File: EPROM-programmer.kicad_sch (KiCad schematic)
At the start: 63 parts, among them J1 ZIF-socket, J2 ISP, J3 DAC_VCC, J4 DAC_B, J5 GND, J6 Barrel_Jack_Switch, J7 VCC_SEL, J8 AMP_VCC, J9 GND, P1 USB-C, Q1 TIP41C, Q2 BC327, Q3 BC337, SW1 SW_Push, U1 ATmega1284-P, U2 MCP2221AxP, U3 MCP4812, U4 LM358, Y1 20M

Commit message: WIP use LM317
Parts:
- removed J7: VCC_SEL, Connector_PinHeader_2.54mm:PinHeader_1x03_P2.54mm_Vertical, symbol Connector:Conn_01x03_Pin
- removed Q1: TIP41C, Package_TO_SOT_THT:TO-220-3_Vertical, symbol Transistor_BJT:TIP41C
- removed Q3: BC337, Package_TO_SOT_THT:TO-92_Inline_Wide, symbol Transistor_BJT:BC337
- removed R18: 2K, Resistor_THT:R_Axial_DIN0207_L6.3mm_D2.5mm_P10.16mm_Horizontal, symbol Device:R
- added C15, C16: 10u, Local:C_Rect_L4.6mm_W3.0mm_P2.50mm_MKS02_FKP02, symbol Device:C_Polarized
- added D8: SB340, Diode_THT:D_DO-201AD_P15.24mm_Horizontal, symbol Diode:B340
- added Q1: BC327, Package_TO_SOT_THT:TO-92_Inline_Wide, symbol Transistor_BJT:BC327
- added U5: ULN2003, Package_DIP:DIP-16_W7.62mm_Socket, symbol Transistor_Array:ULN2003
- added U6: LM317_TO-220, Package_TO_SOT_THT:TO-220-3_Vertical, symbol Regulator_Linear:LM317_TO-220
- J4: value DAC_B -> DAC_VPP
- R15: value 1K -> 5.1K
- R16: value 2K -> 5.1K
- R17: value 2K -> 240
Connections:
- net V_VCC is gone; now on net ZIF_VCC: Q2.1 (C)
- net +28V: now also C15.1, D8.1 (K), U6.3 (VI)
- net AMP_VCC: now also R17.1, C16.1, D8.2 (A), U6.2 (VO)
- net GND: now also C15.2, C16.2, Q1.1 (C), U5.8 (GND)
- net ZIF_VCC_EN: now also U5.1 (I1); no longer R17.1
- net ZIF_VPP_P21_EN: now reaches U1.2 (PB1)
- net ZIF_VPP_P21_EN: now also U5.3 (I3)
- net ZIF_VPP_P22_EN: now reaches U1.3 (PB2)
- net ZIF_VPP_P22_EN: now also U5.5 (I5)
- net ZIF_VPP_P23_EN: now reaches U1.4 (PB3)
- net ZIF_VPP_P23_EN: now also U5.7 (I7)
- net at R15.2: now also U5.16 (O1)
- net at R17.2: now also Q1.3 (E), U6.1 (ADJ)
- net at U4.1: now also Q1.2 (B)
- net DAC_B renamed DAC_VPP
- no-connect marks 10 -> 17
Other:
- moved on the sheet: C12, C6, J1, J5, J8, J9, Q2, R10, R11, R12, R13, R14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

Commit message: Fix some ERC/DRC
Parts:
- added J7: ZIF_VCC, Connector_PinHeader_2.54mm:PinHeader_1x01_P2.54mm_Vertical, symbol Connector:Conn_01x01_Pin
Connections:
- net ZIF_VCC: now also J7.1 (Pin_1)

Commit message: Minor adjustments
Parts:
- R17: value 240 -> 220
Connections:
- net AMP_VCC: no longer R14.2
- net at Q1.3 (E), R17.2, U6.1 (ADJ): now also R14.2
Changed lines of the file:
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@@
 	)
 	(junction
-		(at 154.94 31.75)
-		(diameter 0)
-		(color 0 0 0 0)
-	)
-	(junction
 		(at 190.5 85.09)
 		(diameter 0)
@@
 	)
 	(junction
+		(at 138.43 45.72)
+		(diameter 0)
+		(color 0 0 0 0)
+	)
+	(junction
 		(at 29.21 68.58)
 		(diameter 0)
@@
 	(wire
 		(pts
-			(xy 154.94 31.75) (xy 158.75 31.75)
+			(xy 147.32 31.75) (xy 158.75 31.75)
 		)
 		(stroke
@@
 	(wire
 		(pts
+			(xy 138.43 45.72) (xy 147.32 45.72)
+		)
+		(stroke
+			(width 0)
+			(type default)
+		)
+	)
+	(wire
+		(pts
 			(xy 148.59 187.96) (xy 148.59 189.23)
 		)
@@
 	(wire
 		(pts
+			(xy 138.43 45.72) (xy 129.54 45.72)
+		)
+		(stroke
+			(width 0)
+			(type default)
+		)
+	)
+	(wire
+		(pts
 			(xy 96.52 171.45) (xy 106.68 171.45)
 		)
@@
 	(wire
 		(pts
-			(xy 154.94 31.75) (xy 154.94 63.5)
-		)
-		(stroke
-			(width 0)
-			(type default)
-		)
-	)
-	(wire
-		(pts
 			(xy 271.78 92.71) (xy 271.78 95.25)
 		)
@@
 	(wire
 		(pts
+			(xy 138.43 45.72) (xy 138.43 63.5)
+		)
+		(stroke
+			(width 0)
+			(type default)
+		)
+	)
+	(wire
+		(pts
 			(xy 207.01 148.59) (xy 209.55 148.59)
 		)
@@
 	(wire
 		(pts
-			(xy 147.32 31.75) (xy 154.94 31.75)
-		)
-		(stroke
-			(width 0)
-			(type default)
-		)
-	)
-	(wire
-		(pts
 			(xy 212.09 80.01) (xy 212.09 77.47)
 		)
@@
 	(wire
 		(pts
-			(xy 147.32 45.72) (xy 129.54 45.72)
-		)
-		(stroke
-			(width 0)
-			(type default)
-		)
-	)
-	(wire
-		(pts
 			(xy 123.19 124.46) (xy 115.57 124.46)
 		)
@@
 	(wire
 		(pts
-			(xy 124.46 63.5) (xy 154.94 63.5)
+			(xy 124.46 63.5) (xy 138.43 63.5)
 		)
 		(stroke
@@
 			)
 		)
-		(property "Value" "240"
+		(property "Value" "220"
 			(at 149.86 40.64 0)
 			(effects

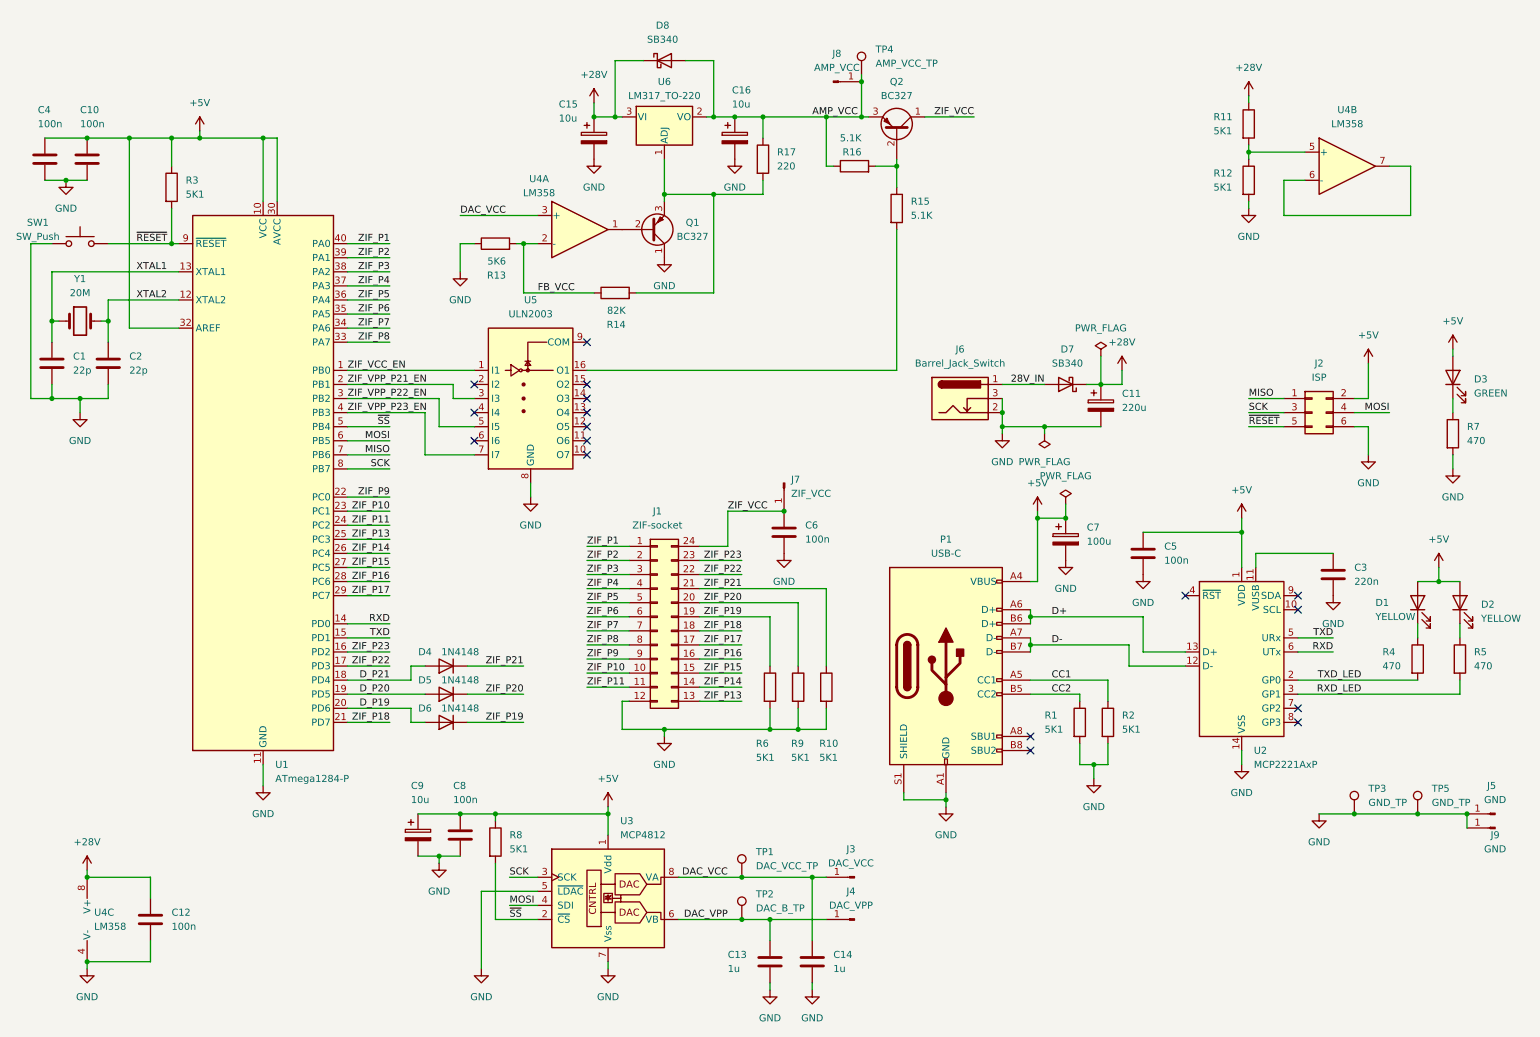
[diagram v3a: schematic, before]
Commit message: Add LM317 for VPP
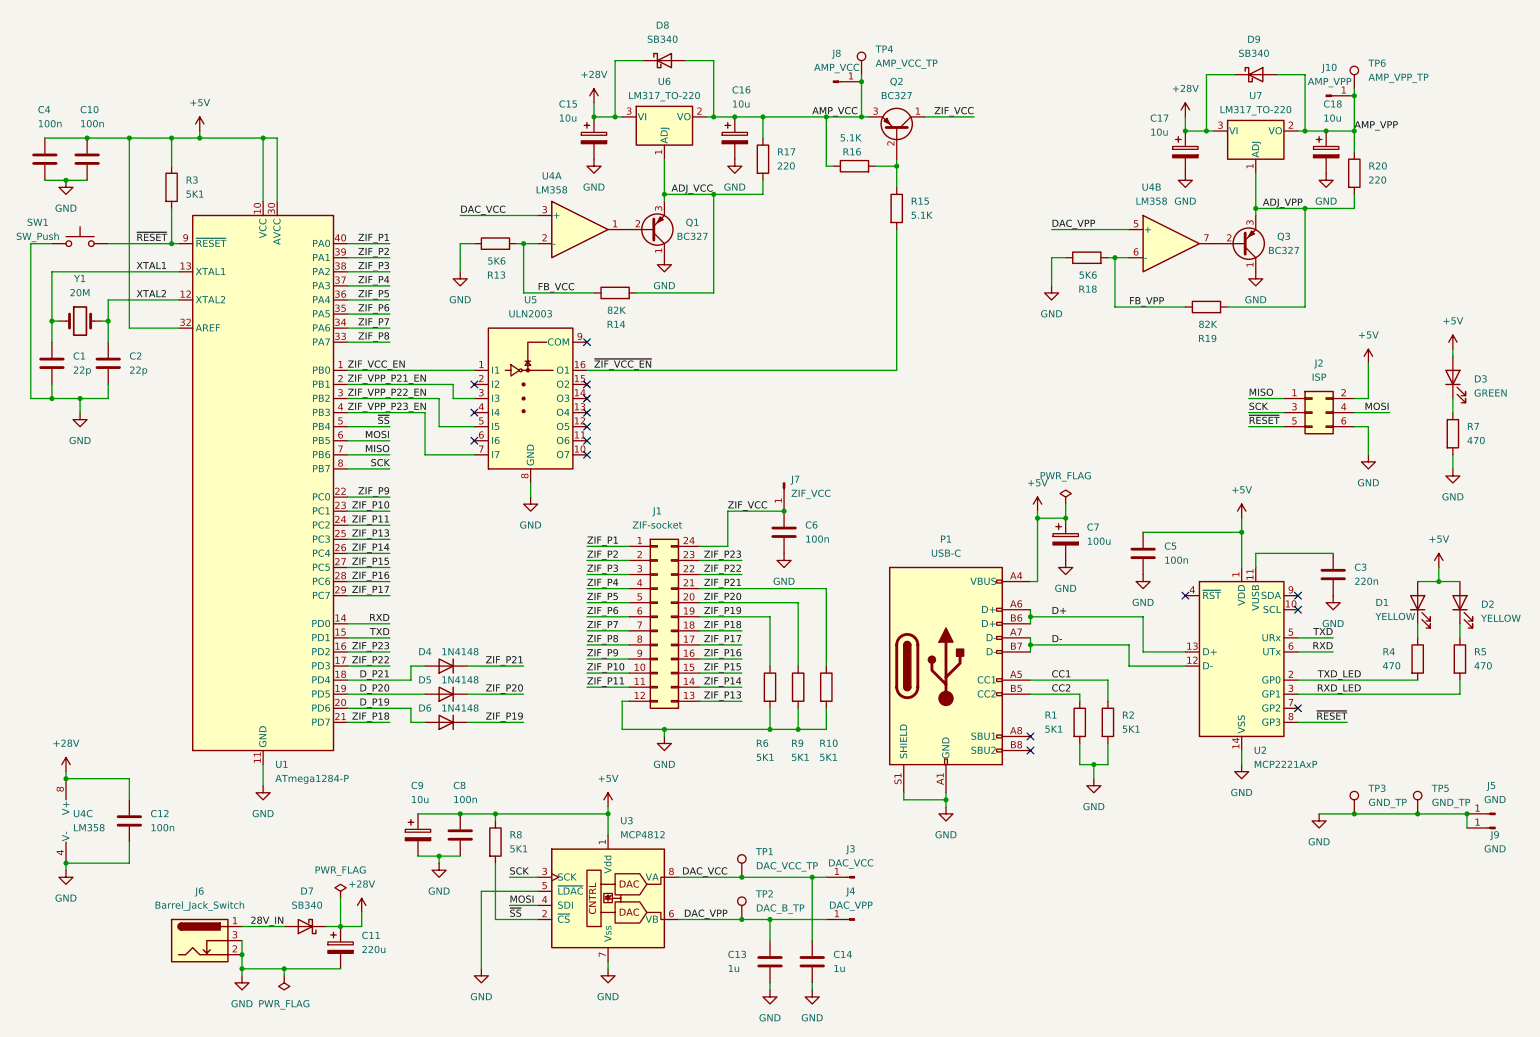
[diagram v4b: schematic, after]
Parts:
- removed R11, R12: 5K1, Resistor_THT:R_Axial_DIN0207_L6.3mm_D2.5mm_P10.16mm_Horizontal, symbol Device:R
- added C17, C18: 10u, Local:C_Rect_L4.6mm_W3.0mm_P2.50mm_MKS02_FKP02, symbol Device:C_Polarized
- added D9: SB340, Diode_THT:D_DO-201AD_P5.08mm_Vertical_KathodeUp, symbol Diode:B340
- added J10: AMP_VPP, Connector_PinHeader_2.54mm:PinHeader_1x01_P2.54mm_Vertical, symbol Connector:Conn_01x01_Pin
- added Q3: BC327, Package_TO_SOT_THT:TO-92_Inline_Wide, symbol Transistor_BJT:BC327
- added R18: 5K6, Resistor_THT:R_Axial_DIN0207_L6.3mm_D2.5mm_P10.16mm_Horizontal, symbol Device:R
- added R19: 82K, Resistor_THT:R_Axial_DIN0207_L6.3mm_D2.5mm_P10.16mm_Horizontal, symbol Device:R
- added R20: 220, Resistor_THT:R_Axial_DIN0207_L6.3mm_D2.5mm_P10.16mm_Horizontal, symbol Device:R
- added TP6: AMP_VPP_TP, TestPoint:TestPoint_Pad_2.0x2.0mm, symbol Connector:TestPoint
- added U7: LM317_TO-220, Package_TO_SOT_THT:TO-220-3_Vertical, symbol Regulator_Linear:LM317_TO-220
- D7, D8: footprint Diode_THT:D_DO-201AD_P15.24mm_Horizontal -> Diode_THT:D_DO-201AD_P5.08mm_Vertical_KathodeUp
- U5: footprint Package_DIP:DIP-16_W7.62mm_Socket -> Package_DIP:DIP-16_W7.62mm
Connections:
- net +28V: now also C17.1, D9.1 (K), U7.3 (VI)
- net DAC_VPP: now also U4.5 (+)
- net GND: now also C17.2, C18.2, Q3.1 (C), R18.1
- net ~{RESET}: now also U2.8 (GP3)
- net ADJ_VCC: now reaches Q1.3 (E), R14.2, R17.2, U6.1 (ADJ)
- net ~{ZIF_VCC_EN}: now reaches R15.2, U5.16 (O1)
- net at U4.7: now also Q3.2 (B); no longer U4.6 (-)
- new net ADJ_VPP: Q3.3 (E), R19.2, R20.2, U7.1 (ADJ)
- new net AMP_VPP: C18.1, D9.2 (A), J10.1 (Pin_1), R20.1, TP6.1, U7.2 (VO)
- new net FB_VPP: R18.2, R19.1, U4.6 (-)
- no-connect marks 17 -> 16
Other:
- moved on the sheet: C11, C12, D7, J6, U4B, U4C

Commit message: Update schematic with the missing VPP-stuff
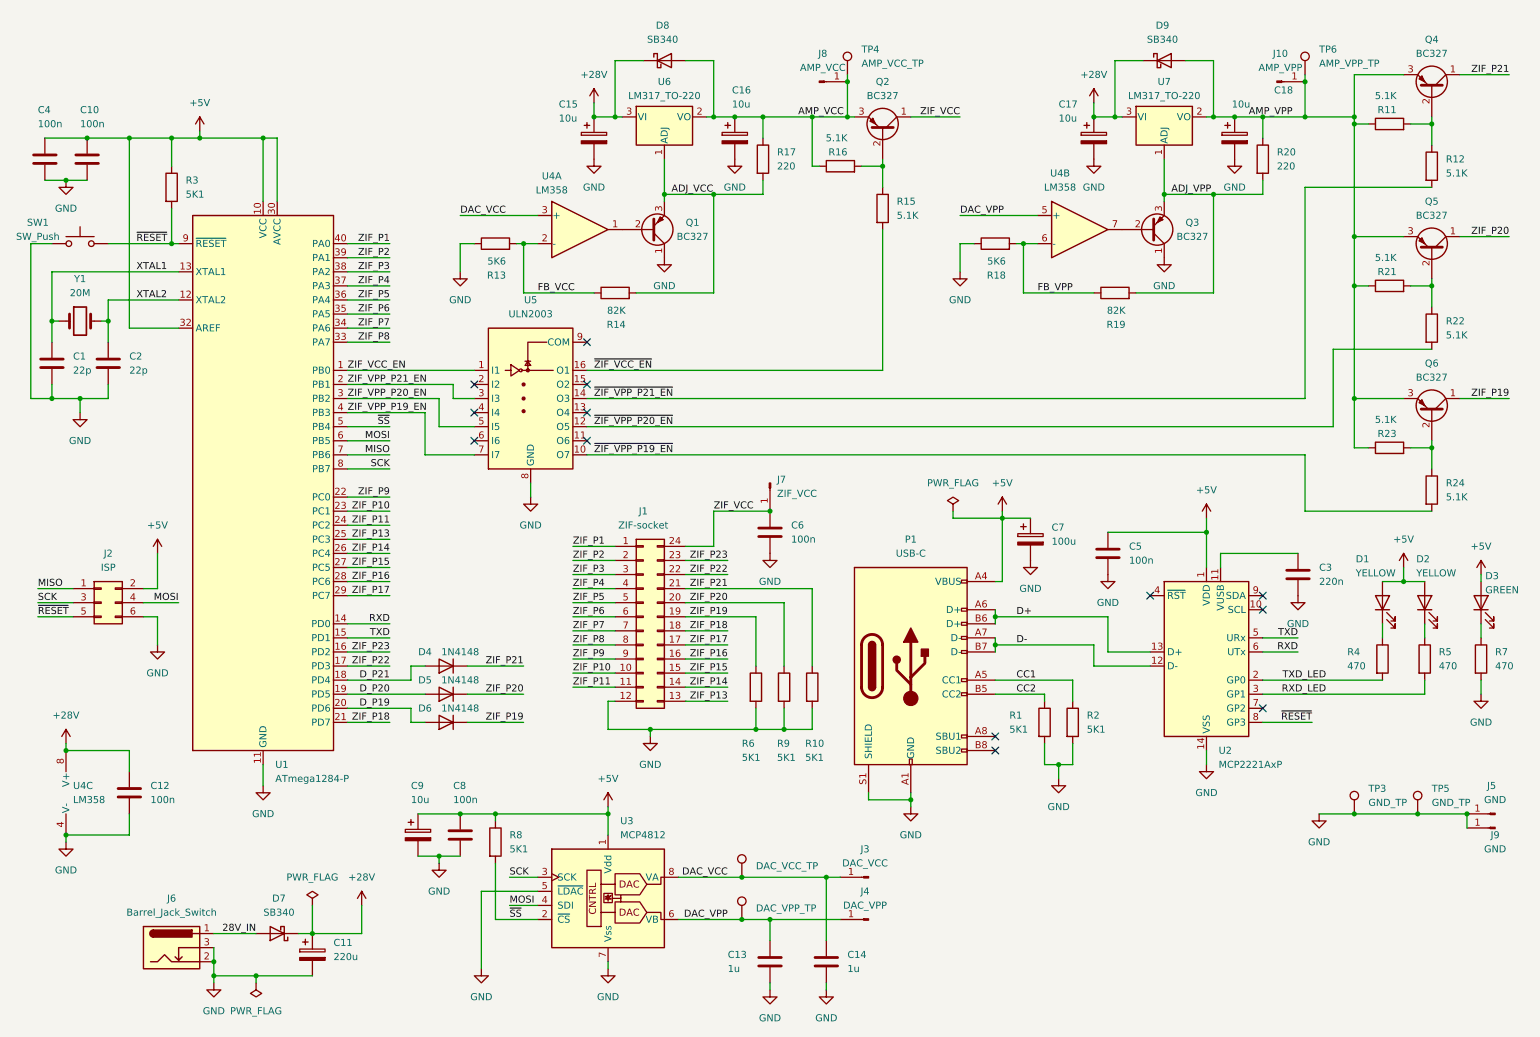
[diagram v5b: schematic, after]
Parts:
- added Q4, Q5, Q6: BC327, Package_TO_SOT_THT:TO-92_Inline_Wide, symbol Transistor_BJT:BC327
- added R11, R12, R21, R22, R23, R24: 5.1K, Resistor_THT:R_Axial_DIN0207_L6.3mm_D2.5mm_P10.16mm_Horizontal, symbol Device:R
- TP2: value DAC_B_TP -> DAC_VPP_TP
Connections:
- net AMP_VPP: now also Q4.3 (E), Q5.3 (E), Q6.3 (E), R11.1, R21.1, R23.1
- net ZIF_P19: now also Q6.1 (C)
- net ZIF_P20: now also Q5.1 (C)
- net ZIF_P21: now also Q4.1 (C)
- net ~{ZIF_VPP_P19_EN}: now reaches U5.10 (O7)
- net ~{ZIF_VPP_P19_EN}: now also R24.2
- net ~{ZIF_VPP_P20_EN}: now reaches U5.12 (O5)
- net ~{ZIF_VPP_P20_EN}: now also R22.2
- net ~{ZIF_VPP_P21_EN}: now reaches U5.14 (O3)
- net ~{ZIF_VPP_P21_EN}: now also R12.2
- net ZIF_VPP_P22_EN renamed ZIF_VPP_P20_EN
- net ZIF_VPP_P23_EN renamed ZIF_VPP_P19_EN
- new net: Q5.2 (B), R21.2, R22.1
- new net: Q4.2 (B), R11.2, R12.1
- new net: Q6.2 (B), R23.2, R24.1
- no-connect marks 16 -> 13
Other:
- moved on the sheet: C11, C12, C14, C17, C18, C3, C5, C6, C7, D1, D2, D3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
